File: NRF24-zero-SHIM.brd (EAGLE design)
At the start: 30 x 65 mm, 33 parts

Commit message: Changed the way how solder joins are organized.
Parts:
- added SJ13, SJ14, SJ15: (no value), _my_jumpers:SJ_2
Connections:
- removed net CSN0: J4.12, SJ10.1, SJ4.1
- removed net CSN1: J4.6, SJ10.3, SJ4.3
- new net CSN00: J4.12, SJ4.2
- new net CSN01: J4.13, SJ13.2
- new net CSN10: J4.6, SJ10.2
- new net CSN11: J3.6, SJ14.2
- new net CSN12: J4.18, SJ15.2
- net CE0: now also SJ5.2; no longer SJ11.1, SJ5.1
- net CE1: now also SJ6.2; no longer SJ11.3, SJ5.3
- net IRQ0: now also SJ11.2; no longer SJ12.1, SJ6.1
- net IRQ1: now also SJ12.2; no longer SJ12.3, SJ6.3
- net MISO0: now also SJ3.2; no longer SJ3.1, SJ9.1
- net MISO1: now also SJ9.2; no longer SJ3.3, SJ9.3
- net MOSI0: now also SJ2.2; no longer SJ2.1, SJ8.1
- net MOSI1: now also SJ8.2; no longer SJ2.3, SJ8.3
- net P0_CE: now also SJ5.1, SJ6.1; no longer SJ5.2
- net P0_CSN: now also SJ10.1, SJ13.1, SJ14.1, SJ15.1, SJ4.1; no longer SJ4.2
- net P0_IRQ: now also SJ11.1, SJ12.1; no longer SJ6.2
- net P0_MISO: now also SJ3.1, SJ9.1; no longer SJ3.2
- net P0_MOSI: now also SJ2.1, SJ8.1; no longer SJ2.2
- net P0_SCK: now also SJ1.1, SJ7.1; no longer SJ1.2
- net P1_CE: now also SJ5.3, SJ6.3; no longer SJ11.2
- net P1_CSN: now also SJ10.3, SJ13.3, SJ14.3, SJ15.3, SJ4.3; no longer SJ10.2
- net P1_IRQ: now also SJ11.3, SJ12.3; no longer SJ12.2
- net P1_MISO: now also SJ3.3, SJ9.3; no longer SJ9.2
- net P1_MOSI: now also SJ2.3, SJ8.3; no longer SJ8.2
- net P1_SCK: now also SJ1.3, SJ7.3; no longer SJ7.2
- net SCK0: now also SJ1.2; no longer SJ1.1, SJ7.1
- net SCK1: now also SJ7.2; no longer SJ1.3, SJ7.3

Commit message: Added zero-sized board.
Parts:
- removed LOGO2: MFDECLOGO_L_20MM, _my_logos:MFDEC_L_20MM
- added SJ16: (no value), _my_jumpers:SJ_2
- moved R8 213.8 mm to (8.13, 20.7), turned to 270 degrees
- moved R7 208.8 mm to (10.7, 20.7), turned to 270 degrees
- moved R6 203.8 mm to (13.2, 20.7), turned to 270 degrees
- moved R5 198.9 mm to (15.7, 20.7), turned to 270 degrees
- moved J1 195.7 mm to (19.6, 29.5), turned to 180 degrees
- moved J2 194.3 mm to (19.6, 26.9), turned to 180 degrees
- moved C3 193.9 mm to (18.3, 20.7), turned to 90 degrees
- moved C4 188.9 mm to (20.8, 20.7), turned to 90 degrees
- moved J5 183.1 mm to (9.40, 35.6)
- moved J6 183.1 mm to (9.40, 38.1)
- moved R2 183.1 mm to (15.7, 44.3)
- moved C1 183.1 mm to (10.7, 44.3)
- moved C2 183.1 mm to (8.13, 44.3)
- moved R1 183.1 mm to (13.2, 44.3)
- moved R3 183.1 mm to (18.3, 44.3)
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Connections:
- new net CE2: J3.7, SJ6.2
- net CE0: now also SJ16.2; no longer SJ5.2
- net CE1: now also SJ5.2; no longer SJ6.2
- net P0_CE: now also SJ16.1
- net P1_CE: now also SJ16.3
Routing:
- net 3.3V: track 0.00 -> 80.0 mm, vias 0 -> 4
- net P1_MISO: track 0.00 -> 73.2 mm, vias 0 -> 5
- net P0_CSN: track 0.00 -> 56.2 mm, vias 0 -> 7
- net P1_SCK: track 0.00 -> 49.1 mm, vias 0 -> 3
- net IRQ0: track 0.00 -> 47.6 mm, vias 0 -> 1
- net P1_CSN: track 0.00 -> 47.2 mm, vias 0 -> 6
- net CSN10: track 0.00 -> 43.7 mm, vias 0 -> 1
- net P1_MOSI: track 0.00 -> 43.5 mm, vias 0 -> 3
- net IRQ1: track 0.00 -> 43.5 mm, vias 0 -> 1
- net CSN11: track 0.00 -> 42.8 mm, vias 0 -> 1
- net P1_CE: track 0.00 -> 40.9 mm, vias 0 -> 4
- net CE1: track 0.00 -> 39.9 mm, vias 0 -> 1
- net P0_SCK: track 0.00 -> 38.8 mm, vias 0 -> 3
- net P0_MOSI: track 0.00 -> 38.1 mm, vias 0 -> 3
- net CSN01: track 0.00 -> 36.8 mm, vias 0 -> 3
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- added copper zone on layer 1, net GND
- added copper zone on layer 16, net GND
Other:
- board text added: "CSN00"
- board text added: "CSN01"
- board text added: "CSN10"
- board text added: "CSN11"
- board text added: "CSN12"
- board text added: "IO27"
- board text added: "NRF24-zero-SHIM v1.0"
- board text added: "P0"
- board text added: "P1"
- board text added: "SPI0 bus selection CE select."
- board text added: "SPI1 bus selection IRQ sel."
- board text removed: "CSN0"
- board text removed: "CSN1"
- board text removed: "NRF24-SHIM v1.0"
- board text removed: "SPI bus select. CE IRQ"

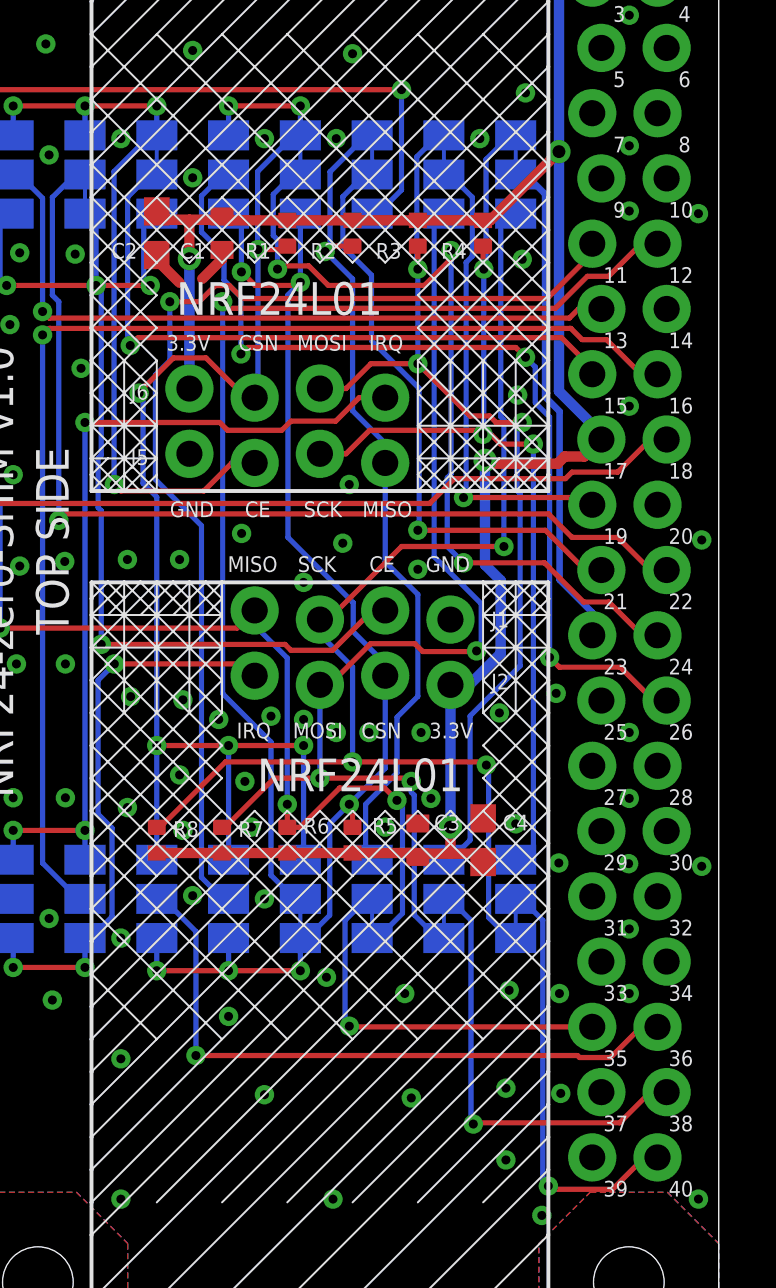
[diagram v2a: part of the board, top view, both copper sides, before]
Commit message: Moved some traces and vias to allow better ground surface. Generated new PNG preview. Generated new CAM.
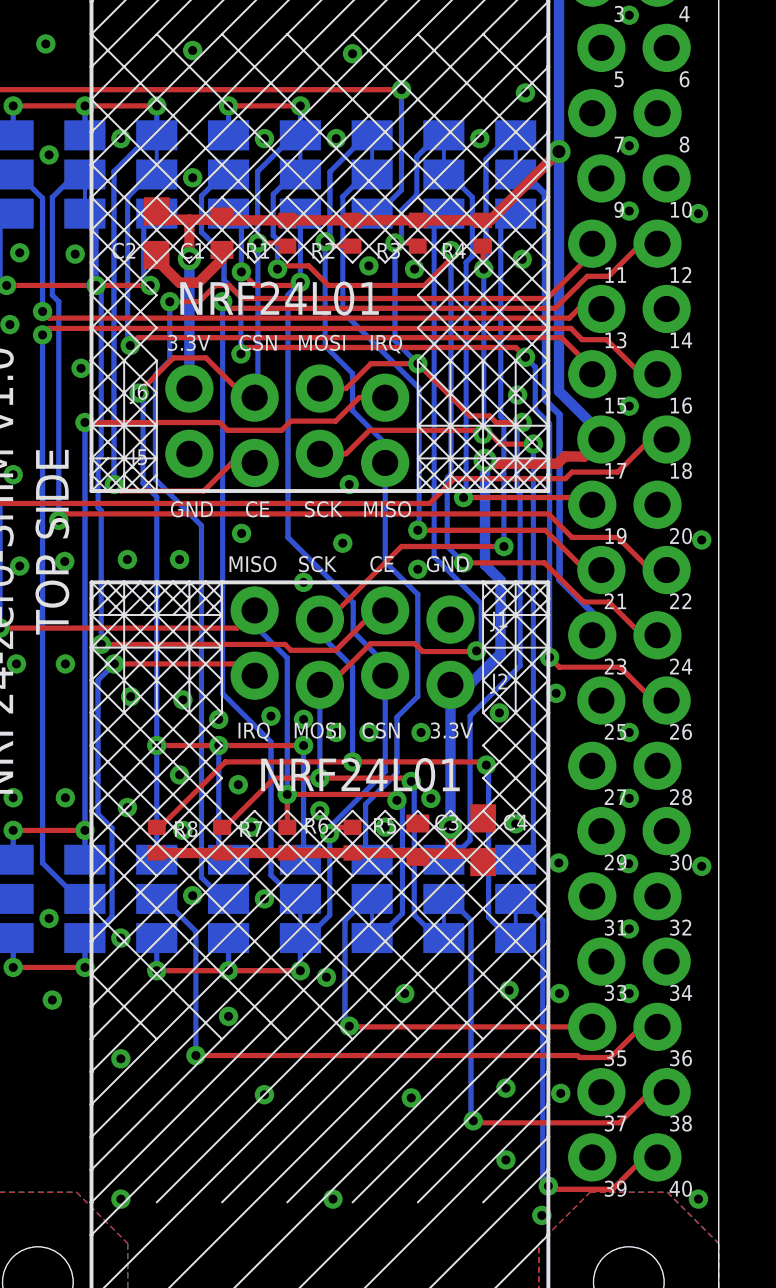
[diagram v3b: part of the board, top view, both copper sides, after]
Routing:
- net GND: track 2.88 -> 3.84 mm, vias 97 -> 100
- net P0_MOSI: track 38.1 -> 38.9 mm
- net P1_MISO: track 73.2 -> 72.5 mm
